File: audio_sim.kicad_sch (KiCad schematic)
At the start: 15 parts, among them U1 ${SIM.PARAMS}

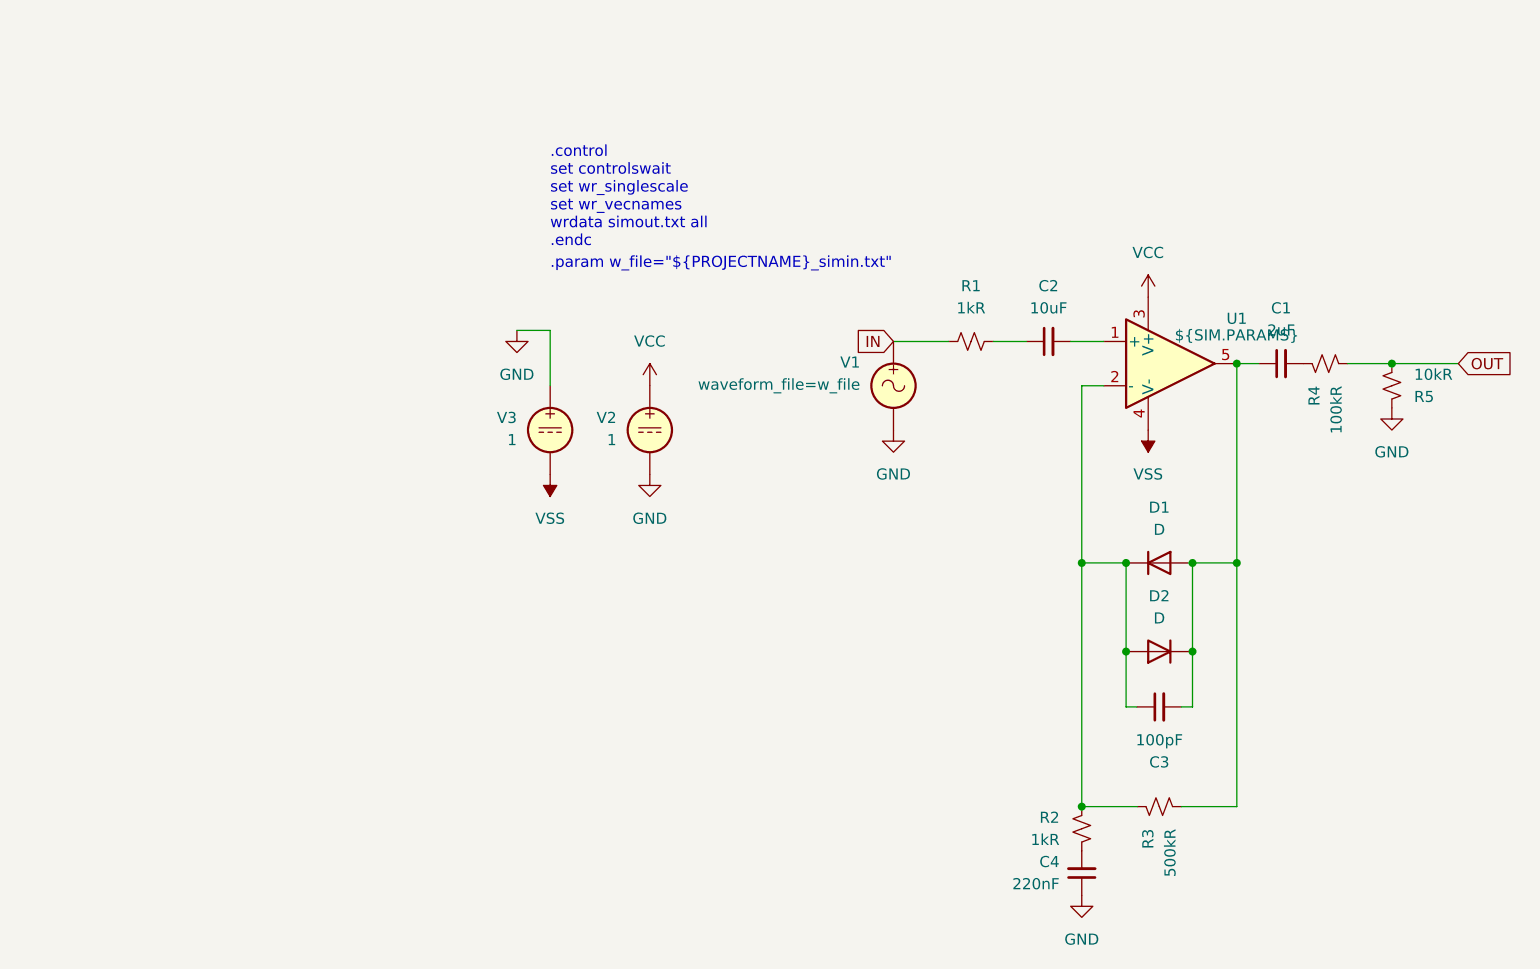
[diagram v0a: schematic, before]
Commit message: Added Phaser pedal
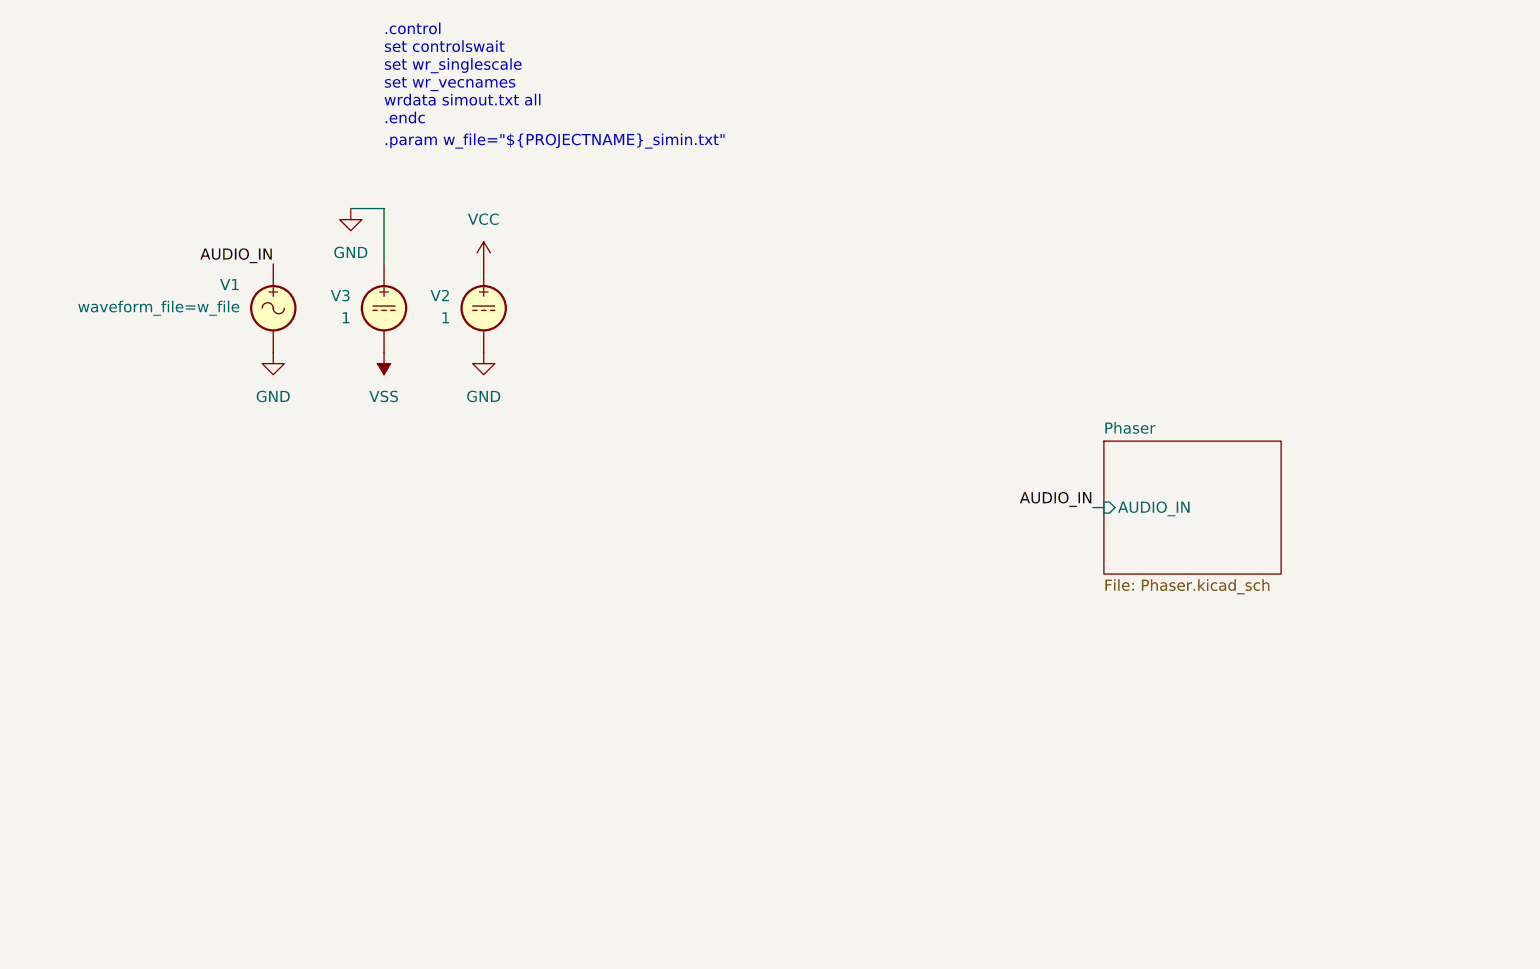
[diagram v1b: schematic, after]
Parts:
- removed C1: 2uF, symbol Device:C_Small
- removed C2: 10uF, symbol Device:C_Small
- removed C3: 100pF, symbol Device:C_Small
- removed C4: 220nF, symbol Device:C_Small
- removed D1, D2: D, symbol Device:D
- removed R1, R2: 1kR, symbol Device:R_Small_US
- removed R3: 500kR, symbol Device:R_Small_US
- removed R4: 100kR, symbol Device:R_Small_US
- removed R5: 10kR, symbol Device:R_Small_US
- removed U1: ${SIM.PARAMS}, symbol Simulation_SPICE:OPAMP
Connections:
- net IN renamed AUDIO_IN
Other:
- added sheet Phaser (Phaser.kicad_sch)
- moved on the sheet: V1, V2, V3
